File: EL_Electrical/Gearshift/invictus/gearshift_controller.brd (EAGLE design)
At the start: 160 x 100 mm, 65 parts, among them IC1 MCP2562-E_SN, IC2 MCP2515-I_SO, Q1 BSS138, Q10 BSS138, Q2 BSS138, Q3 BSS138, Q4 BSS138, Q5 BSS138, Q6 BSS138, Q8 BSS138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

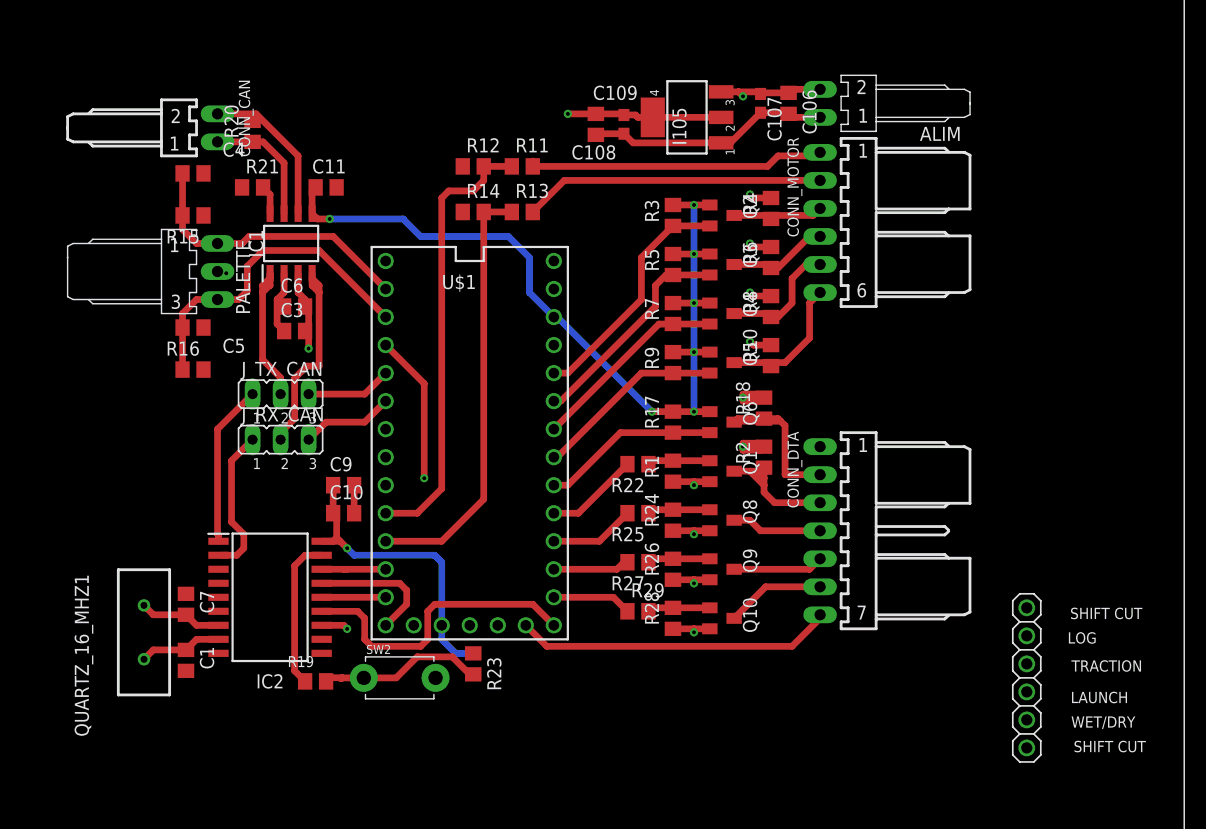
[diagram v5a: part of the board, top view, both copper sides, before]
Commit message: Replace pin test
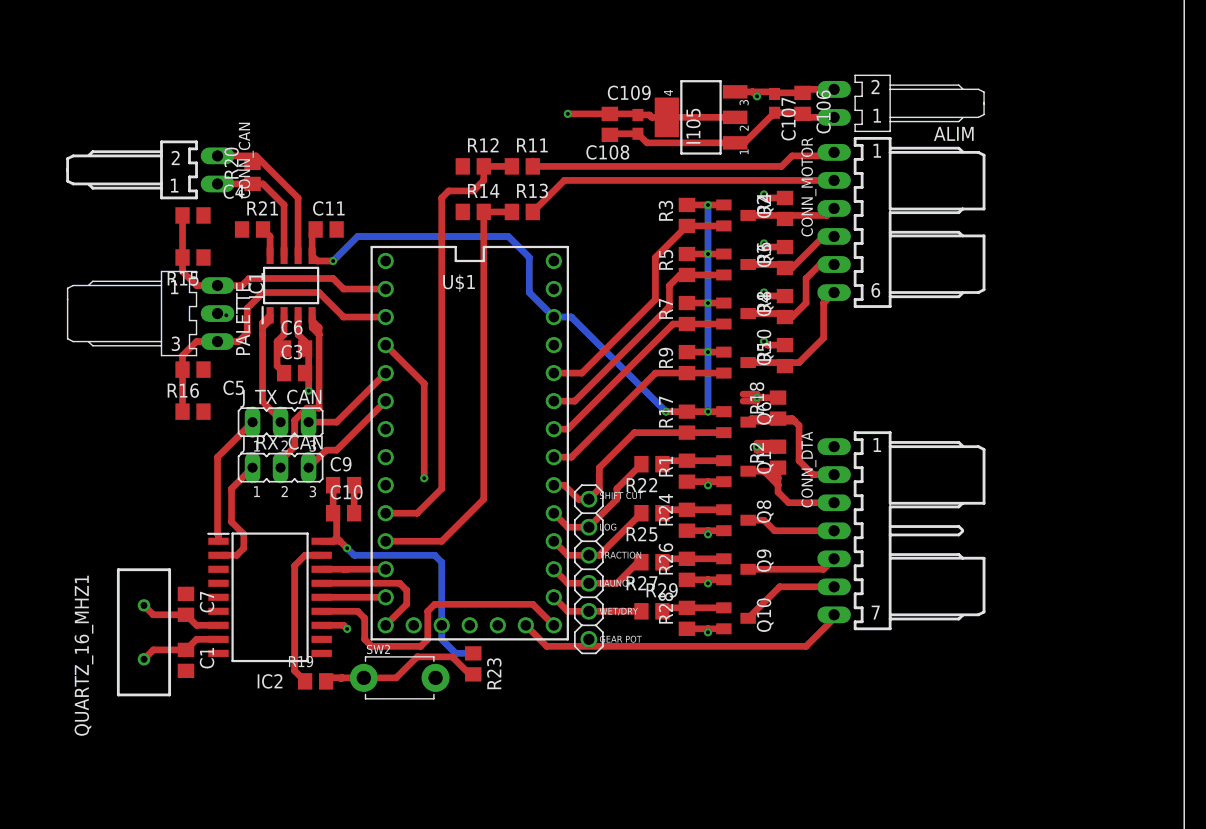
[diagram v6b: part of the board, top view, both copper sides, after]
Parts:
- moved TEST_DTA 40.9 mm to (106.0, 38.7)
- moved C11 3.81 mm to (82.2, 69.5)
- moved C3 3.81 mm to (79.4, 56.5)
- moved C4 3.81 mm to (70.2, 70.8)
- moved C5 3.81 mm to (70.2, 53.0)
- moved C6 3.81 mm to (79.4, 58.7)
- moved IC1 3.81 mm to (79.1, 64.5)
- moved R20 3.81 mm to (75.6, 74.6)
- moved R21 3.81 mm to (75.6, 69.5)
- moved PALETTE 3.81 mm to (72.4, 61.9)
- moved R16 3.81 mm to (70.2, 56.8)
- moved CONN_CAN 3.81 mm to (72.4, 74.9)
- moved R15 3.81 mm to (70.2, 67.0)
- moved J_RX_CAN 2.54 mm to (78.1, 47.9)
- moved J_TX_CAN 2.54 mm to (78.1, 52.1)
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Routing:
- net +5V: track 122.3 -> 133.1 mm
- net SHIFT_CUT_3.3V: track 16.1 -> 19.6 mm
- net LOG_3.3V: track 8.51 -> 11.4 mm
- net CAN-TXD-SOFTWARE: track 14.7 -> 12.1 mm
- net CAN-RXD_SOFTWARE: track 13.4 -> 10.9 mm
- net TRACTION_CONTROL_3.3V: track 7.72 -> 10.0 mm
- net LAUNCH_CONTROL_3.3V: track 6.93 -> 9.26 mm
- net TX_CAN: track 14.0 -> 12.0 mm
- net PALETTE_DROITE: track 29.7 -> 28.1 mm
- net PALETTE_GAUCHE: track 26.3 -> 24.7 mm
- net +3V3: track 107.0 -> 108.6 mm
- net IN1_12V: track 27.5 -> 28.8 mm
- net GEAR_POT: track 28.8 -> 30.1 mm
- net RX_CAN: track 19.0 -> 17.7 mm
- net OUT2_3.3V: track 20.0 -> 21.3 mm
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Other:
- board text added: "GEAR POT"

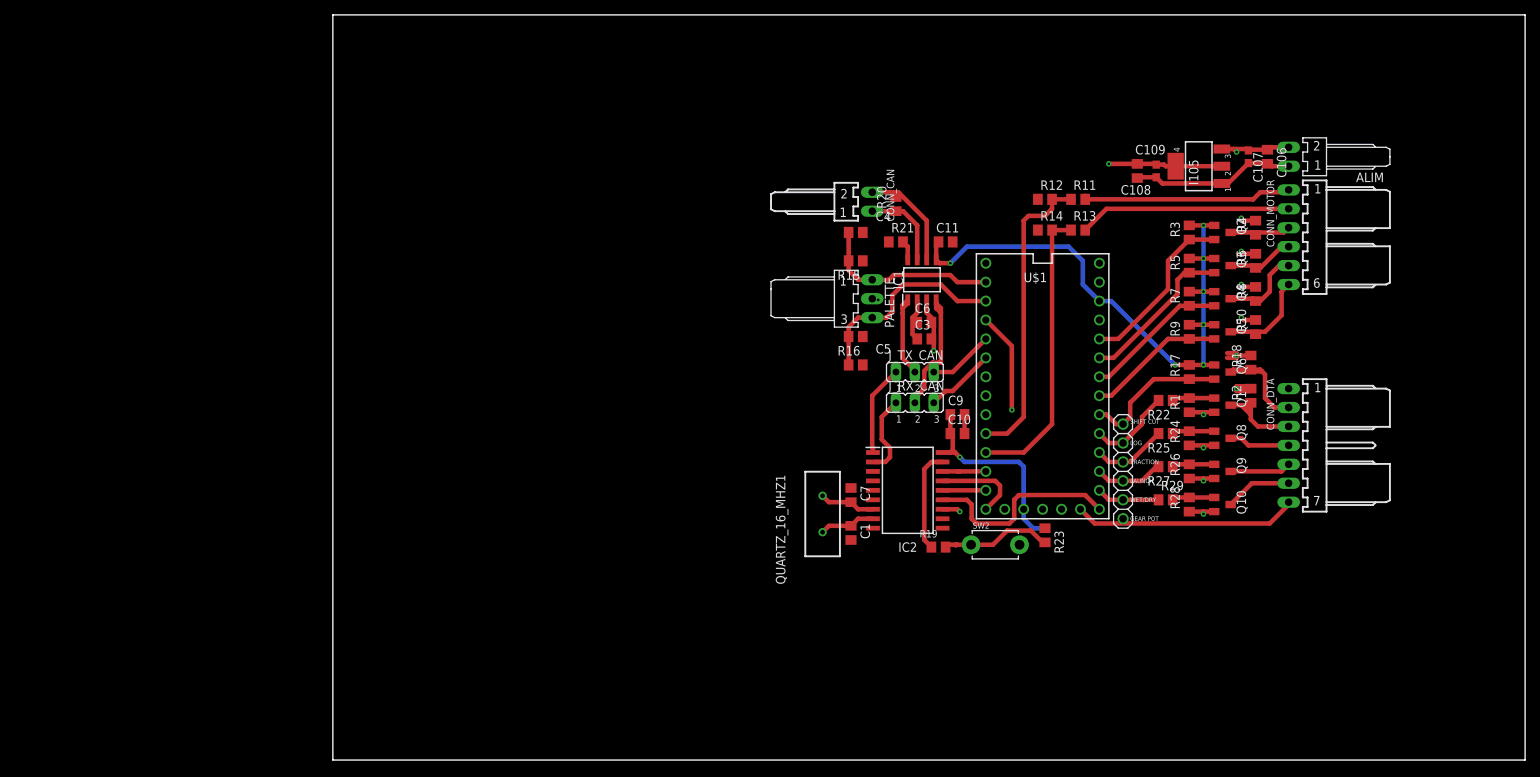
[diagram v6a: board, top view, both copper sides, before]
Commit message: Ground plane for gearshift. Add dashboard
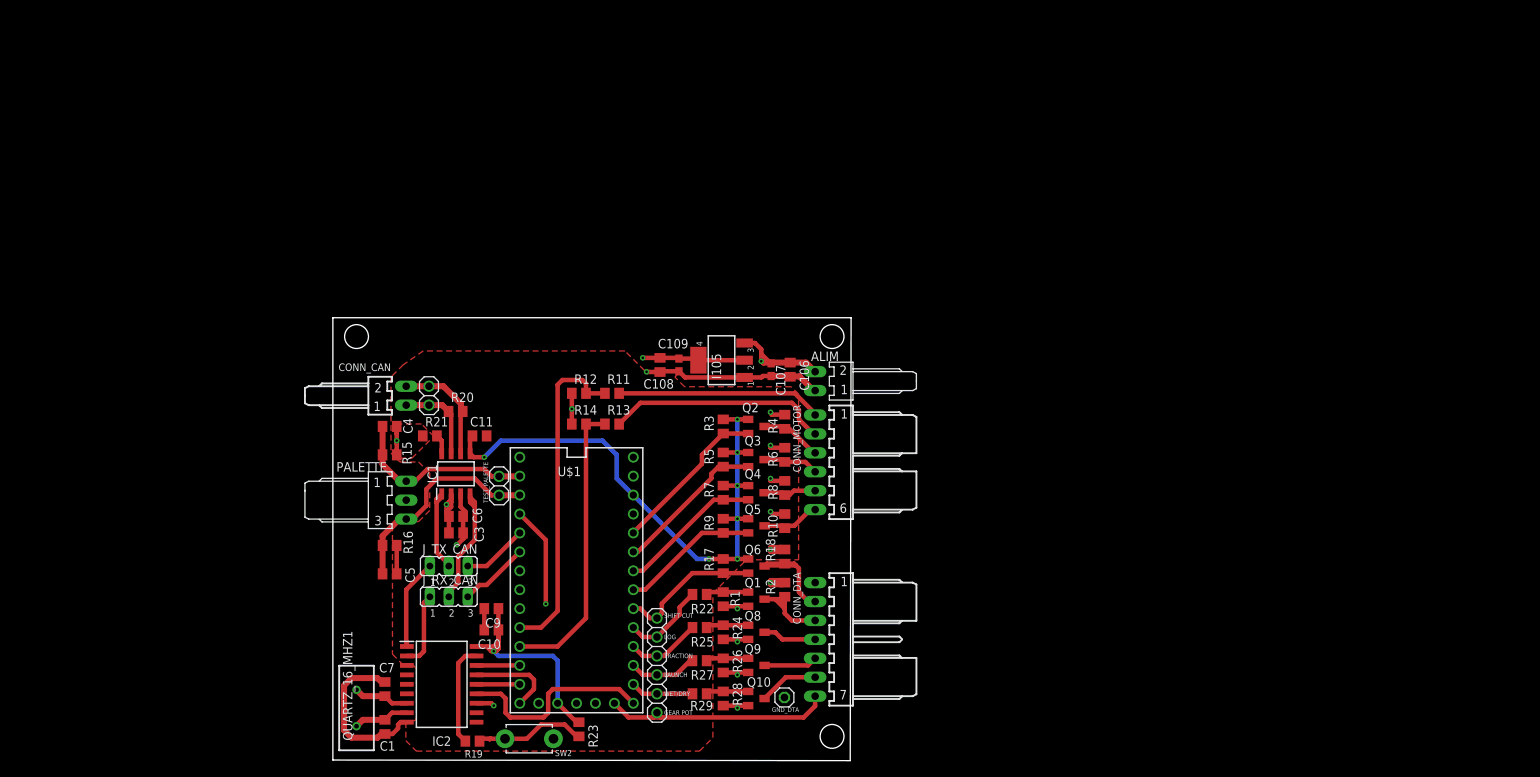
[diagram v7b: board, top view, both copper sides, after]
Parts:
- added GND_DTA: (no value), pinhead:1X01
- added TEST_CAN, TEST_PALETTE: (no value), test_pin_DTA:1X02
- moved CONN_MOTOR 70.4 mm to (64.7, 40.0)
- moved ALIM 70.3 mm to (64.7, 50.9)
- moved C107 70.1 mm to (58.8, 52.4)
- moved C106 70.1 mm to (61.4, 52.4)
- moved C108 69.1 mm to (43.9, 53.0)
- moved I105 69.1 mm to (52.2, 53.7)
- moved C109 69.1 mm to (46.4, 53.0)
- moved CONN_DTA 68.7 mm to (64.7, 16.2)
- moved C5 68.5 mm to (7.62, 25.0)
- moved R16 68.5 mm to (7.62, 28.8)
- moved R10 68.3 mm to (60.6, 32.1)
- moved R4 68.3 mm to (60.6, 45.4)
- moved R6 68.3 mm to (60.6, 41.0)
- moved R8 68.3 mm to (60.6, 36.5)
- moved PALETTE 68.1 mm to (9.84, 34.9)
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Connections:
- net GND: now also GND_DTA.1
- net N$4: now also TEST_CAN.1
- net N$6: now also TEST_CAN.2
- net PALETTE_DROITE: now also TEST_PALETTE.2
- net PALETTE_GAUCHE: now also TEST_PALETTE.1
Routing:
- net GND: track 30.8 -> 75.4 mm, vias 0 -> 4
- net GND1: track 31.5 -> 39.8 mm
- net +12V: track 41.1 -> 45.9 mm
- net +3V3: track 108.6 -> 113.1 mm
- net OUT4_12V: track 12.3 -> 8.14 mm
- net OUT3_12V: track 11.2 -> 7.16 mm
- net IN0_3.3V: track 40.6 -> 44.5 mm
- net N$4: track 11.4 -> 15.0 mm
- net OUT2_12V: track 9.10 -> 7.47 mm
- net OUT1_3.3V: track 23.2 -> 21.7 mm
- net GEAR_POT: track 30.1 -> 31.4 mm
- net IN1_12V: track 28.8 -> 30.0 mm
- net N$6: track 14.1 -> 15.1 mm
- net LOG_5V: track 12.5 -> 11.5 mm
- net WET/DRY: track 8.97 -> 7.97 mm
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- added copper zone on layer 15, net +5V
- added copper zone on layer 1, net GND
- added copper zone on layer 2, net GND
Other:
- board size 160 x 100 mm -> 69.5 x 59.4 mm

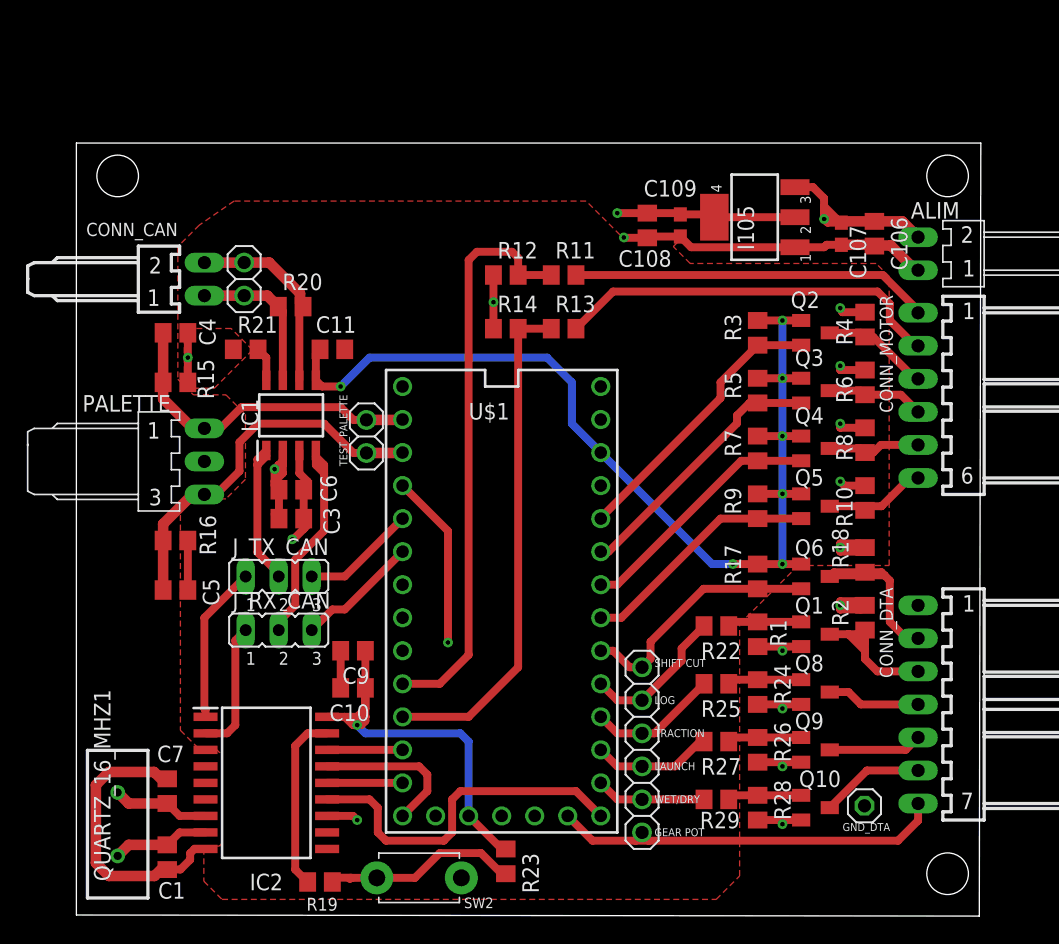
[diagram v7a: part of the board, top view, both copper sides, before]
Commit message: Add capacitors (470uF: about 18,20mm x 10,8mm; Footprint utilisé 25mm x 10mm)
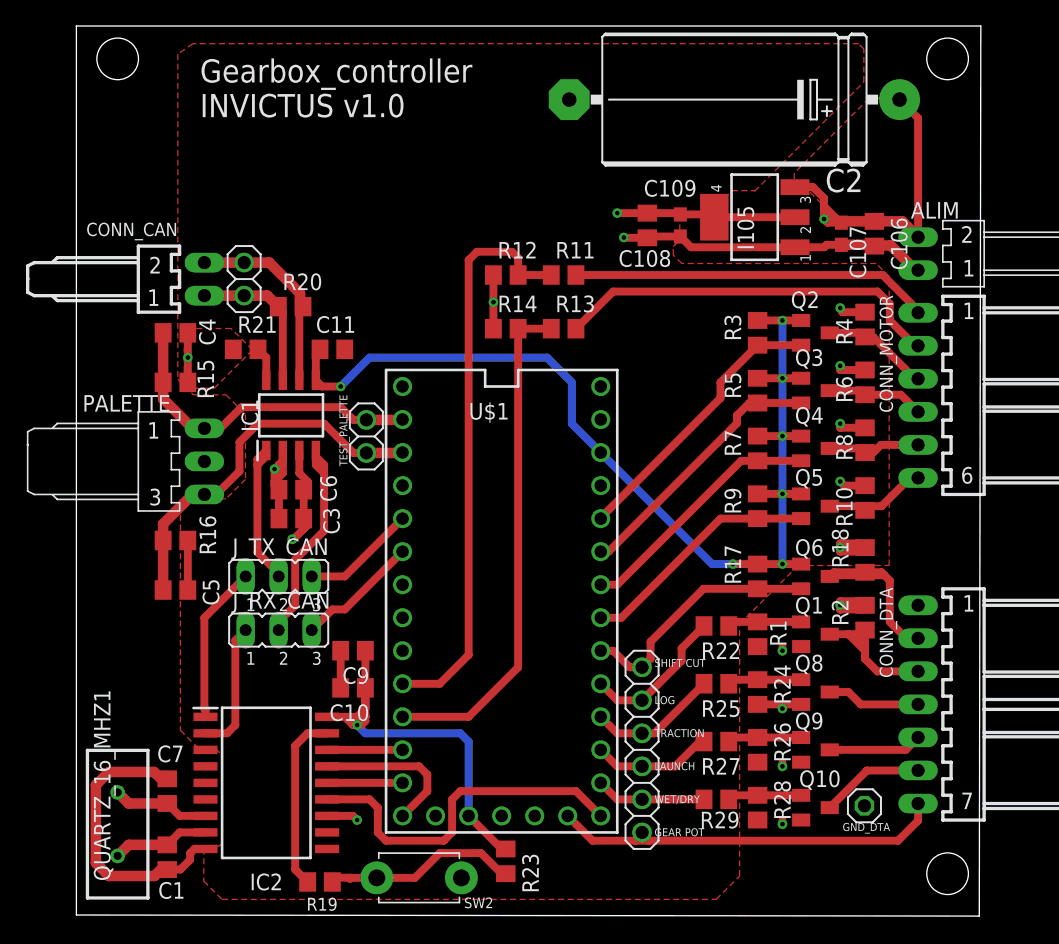
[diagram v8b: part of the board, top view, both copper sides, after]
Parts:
- added C2: 1000uF, rcl:E25-10
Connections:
- removed net GND1: CONN_DTA.1, Q1.2, Q10.2, Q8.2, Q9.2, R1.1, R24.1, R26.1, R28.1
- net +12V: now also C2.+
- net GND: now also C2.-, CONN_DTA.1, Q1.2, Q10.2, Q8.2, Q9.2, R1.1, R24.1, R26.1, R28.1
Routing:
- net GND1: track 39.8 -> 0.00 mm, vias 4 -> 0
- net GND: track 75.4 -> 100.1 mm, vias 4 -> 8
- net +12V: track 45.9 -> 57.1 mm
- net INT: vias 2 -> 1
- added copper zone on layer 1, net +12V
- removed copper zone on layer 2, net GND1
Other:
- board size 69.5 x 59.4 mm -> 69.5 x 68.4 mm
- board text added: "Gearbox_controller INVICTUS v1.0"
